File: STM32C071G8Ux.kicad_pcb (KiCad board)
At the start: 4 copper layers, 16 x 47.5 mm, 35 parts, among them J1 UJ20-C-H-G-SMT-1-P16-TR, J2 Conn_01x14, J3 Conn_01x14, J4 Conn_ARM_SWD_TagConnect_TC203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, J5 Conn_ARM_JTAG_SWD_10, U1 STM32C071G8Ux, U2 USBLC6-2SC6, U4 TLV75533PDBV

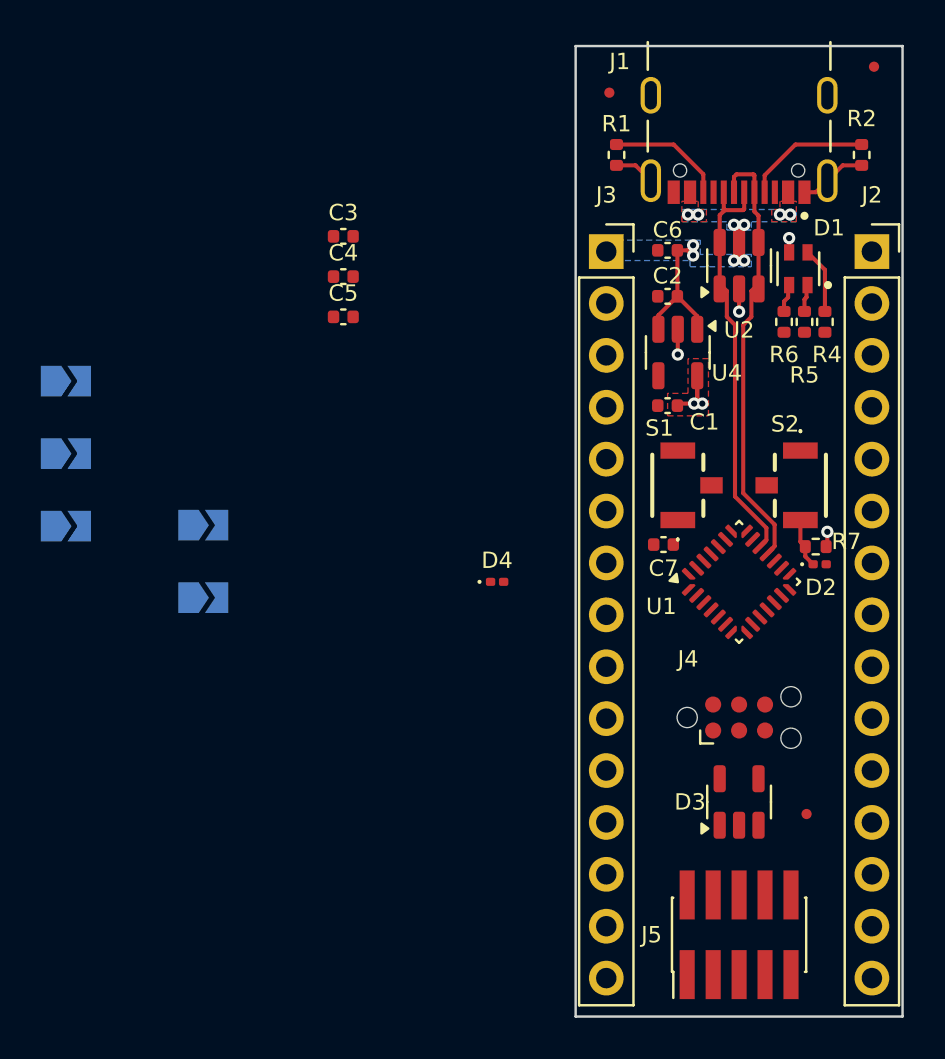
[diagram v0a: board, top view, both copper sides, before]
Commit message: routing done but drc errors
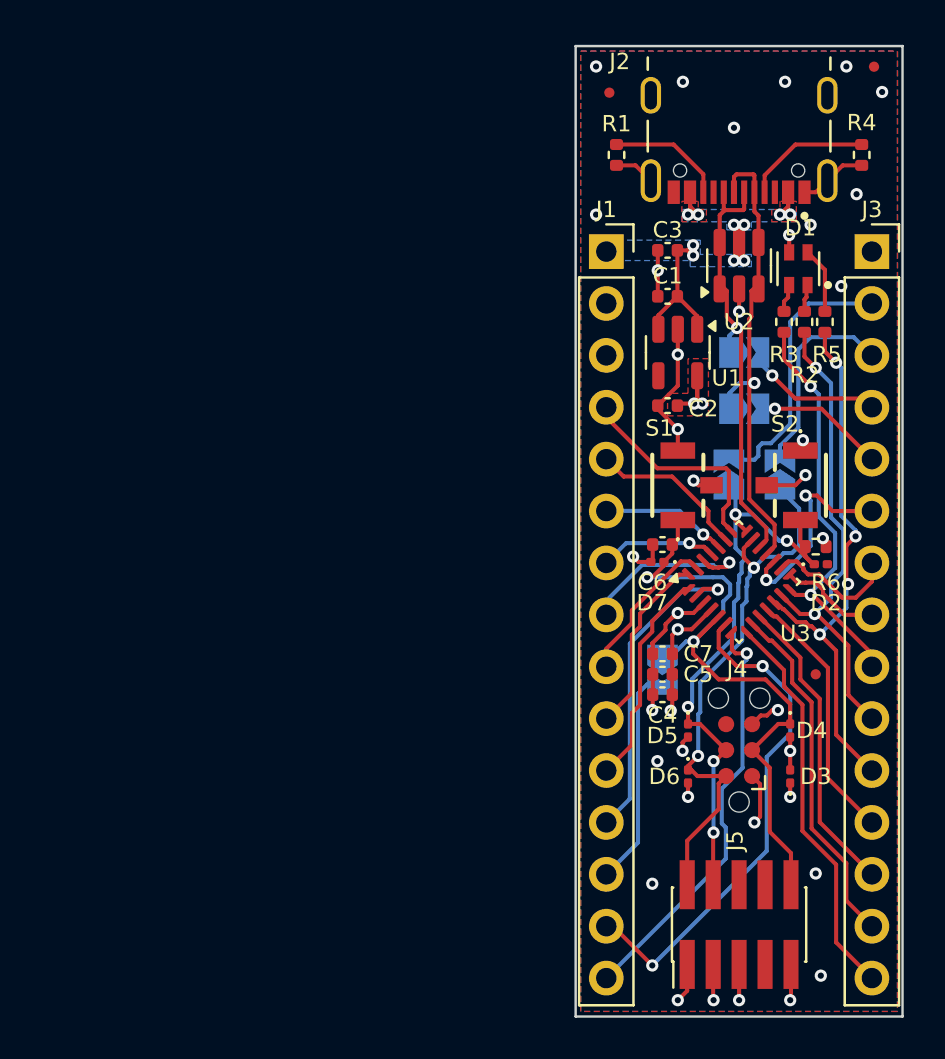
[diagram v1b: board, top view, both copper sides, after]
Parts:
- added D4: ESDALC6V1-1U2, Diode_SMD:D_0201_0603Metric, F.Cu at (135.8, 101.2)
- added D5: ESDALC6V1-1U2, Diode_SMD:D_0201_0603Metric, F.Cu at (130.8, 101.2)
- added D6: ESDALC6V1-1U2, Diode_SMD:D_0201_0603Metric, F.Cu at (130.8, 103.5)
- D3: value ESDALC6V1W5 -> ESDALC6V1-1U2; footprint Package_TO_SOT_SMD:SOT-23-5 -> Diode_SMD:D_0201_0603Metric
- moved JP1 35.0 mm to (135.3, 88.7), turned to 90 degrees
- moved JP2 32.5 mm to (132.8, 88.7), turned to 90 degrees
- moved JP5 32.4 mm to (129.6, 98.3), turned to -90 degrees
- moved JP3 29.1 mm to (133.6, 82.7)
- moved C4 27.3 mm to (129.6, 99.5)
- moved JP4 27.1 mm to (133.6, 85.5)
- moved C7 24.2 mm to (129.6, 97.5)
- moved C5 23.5 mm to (129.6, 98.5)
- moved D7 7.91 mm to (129.3, 93.0), turned to 180 degrees
- moved FID3 6.85 mm to (137.1, 98.5)
- moved D3 2.80 mm to (135.8, 103.5)
- moved J4 1.59 mm to (133.3, 102.2), turned to 90 degrees
- moved J5 0.50 mm to (133.3, 110.7)
- moved D2 0.06 mm to (137.3, 93.1)
- moved C6 0.05 mm to (129.6, 92.1)
- renumbered C2 to C1, C1 to C2, C6 to C3, C3 to C4, C7 to C6, C4 to C7, D4 to D7, J3 to J1, J1 to J2, J2 to J3, JP4 to JP1, JP5 to JP2, JP2 to JP3, JP1 to JP4, JP3 to JP5, R5 to R2, R6 to R3, R2 to R4, R4 to R5, R7 to R6, U4 to U1, U1 to U3
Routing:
- net DEBUG_RESET: track 0.00 -> 33.8 mm, vias 0 -> 2
- net GND: track 8.88 -> 37.4 mm, vias 3 -> 31
- net BOOT0: track 2.42 -> 30.5 mm, vias 0 -> 5
- net DEBUG_SWDIO: track 0.00 -> 26.9 mm, vias 0 -> 2
- net PA6: track 0.00 -> 26.8 mm, vias 0 -> 4
- net PA0: track 0.00 -> 24.9 mm, vias 0 -> 2
- net PA7: track 0.00 -> 23.5 mm, vias 0 -> 2
- net PA1: track 0.00 -> 20.6 mm, vias 0 -> 1
- net PB0: track 0.00 -> 20.5 mm, vias 0 -> 2
- net PA2: track 0.00 -> 19.5 mm
- net PA3: track 0.00 -> 17.3 mm
- net PC15: track 0.00 -> 15.8 mm, vias 0 -> 1
- net PA4: track 0.00 -> 14.9 mm
- net PA14: track 0.00 -> 13.4 mm
- net +3V3: track 4.45 -> 17.2 mm, vias 3 -> 9
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- added copper zone on B.Cu, net GND
- added copper zone on F.Cu, net GND

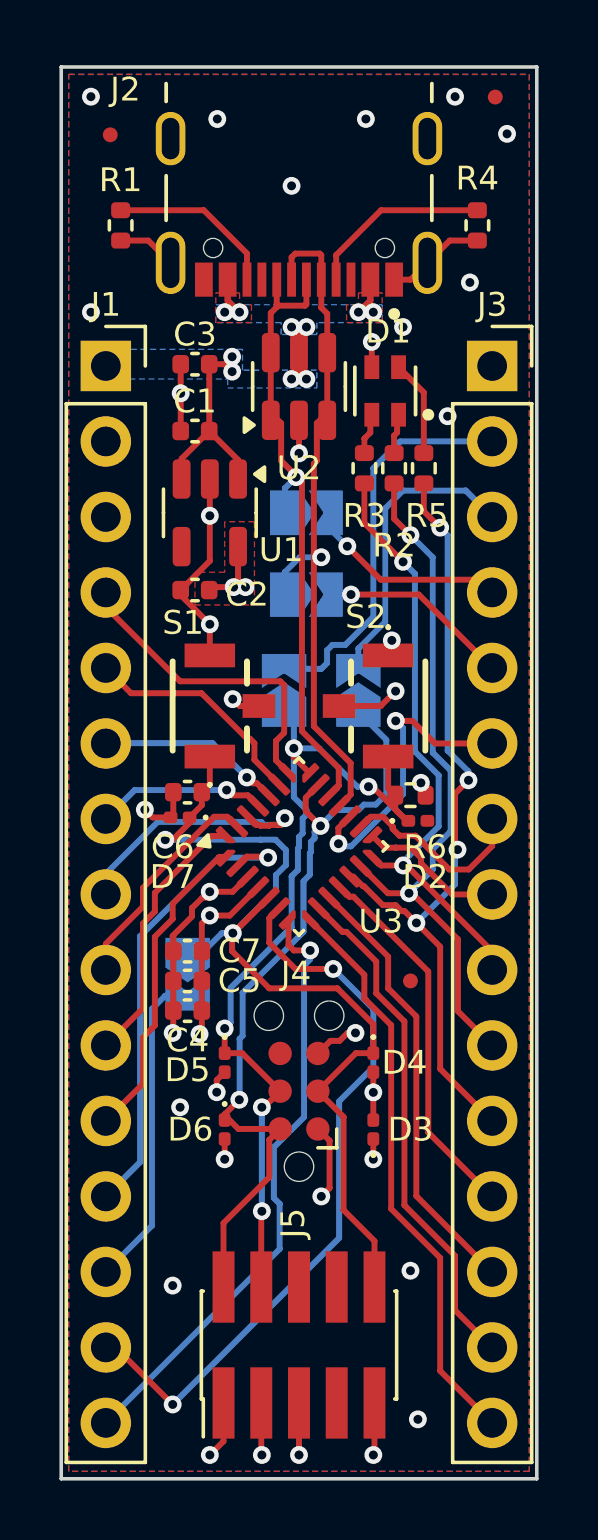
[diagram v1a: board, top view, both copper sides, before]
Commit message: fixed some design rules
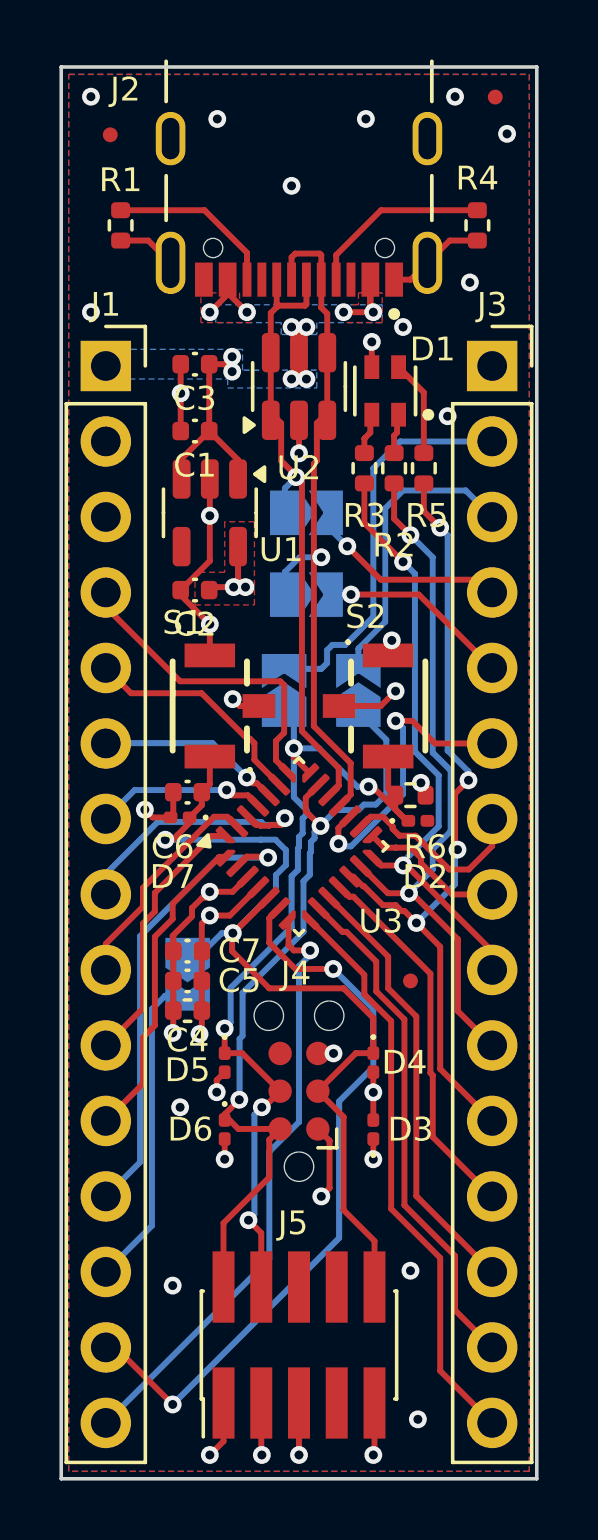
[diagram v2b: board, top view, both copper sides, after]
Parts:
- C1, C2, C3, C5, C6, C7: footprint Capacitor_SMD:C_0402_1005Metric -> footprints:C_0402_1005Metric
- JP1, JP2, JP3, JP4, JP5: footprint Jumper:SolderJumper-2_P1.3mm_Open_TrianglePad1.0x1.5mm -> footprints:SolderJumper-2_P1.3mm_Open_TrianglePad1.0x1.5mm
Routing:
- net VCC: track 14.9 -> 15.9 mm
- net GND: track 37.4 -> 36.4 mm
